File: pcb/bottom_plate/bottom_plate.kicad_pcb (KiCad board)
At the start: 2 copper layers, 285.8 x 126.1 mm, 44 parts

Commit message: Remove redundant ESD protection from bottom plate.
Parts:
- removed U_ESD_D1, U_ESD_D2, U_ESD_D3, U_ESD_D4, U_ESD_D5: CM1293A, Package_TO_SOT_SMD:SOT-23-6
- H1, H10, H11, H12, H2, H3, H4, H5, H6, H7, H8, H9: footprint MountingHole:MountingHole_2.2mm_M2 -> MountingHole:MountingHole_2.2mm_M2_Pad
- moved C1 4.36 mm to (239.4, 90.0)
- moved C2 4.36 mm to (241.9, 90.0)
- moved D_POW_1 4.36 mm to (242.9, 79.5)
- moved JP_CHG_1 4.36 mm to (241.9, 74.2)
- moved Q_POW_1 4.36 mm to (241.4, 84.5)
- moved R_CHG_1 4.36 mm to (238.3, 73.3)
- moved R_CHG_2 4.36 mm to (238.3, 68.3)
- moved R_POW_1 4.36 mm to (244.4, 90.0)
- moved U_CHG_1 4.36 mm to (238.4, 79.5)
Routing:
- net /Left/VCC: track 213.2 -> 171.5 mm, vias 6 -> 5
- net /Left/SCLK: track 181.1 -> 141.4 mm, vias 4 -> 5
- net /Right/CS_DIS2: track 60.9 -> 29.0 mm
- net /Left/MISO: track 175.8 -> 145.1 mm, vias 4 -> 5
- net /Left/VDD: track 189.8 -> 217.0 mm, vias 8 -> 5
- net /Left/CS_DIS2: track 120.2 -> 98.2 mm, vias 2 -> 0
- net /Left/GND: track 69.0 -> 48.4 mm, vias 22 -> 12
- net /Left/D-: track 112.0 -> 98.4 mm
- net /Left/MOSI: track 161.2 -> 148.4 mm, vias 6 -> 5
- net /Right/MISO: track 70.4 -> 60.2 mm
- net /Left/RST: track 164.8 -> 155.3 mm
- net /Left/SDA: track 145.1 -> 154.5 mm, vias 6 -> 5
- net /Left/D+: track 107.5 -> 98.4 mm
- net /Right/VDD: track 47.8 -> 40.1 mm
- net /Left/CS_PMW2: track 124.1 -> 117.2 mm, vias 2 -> 0
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
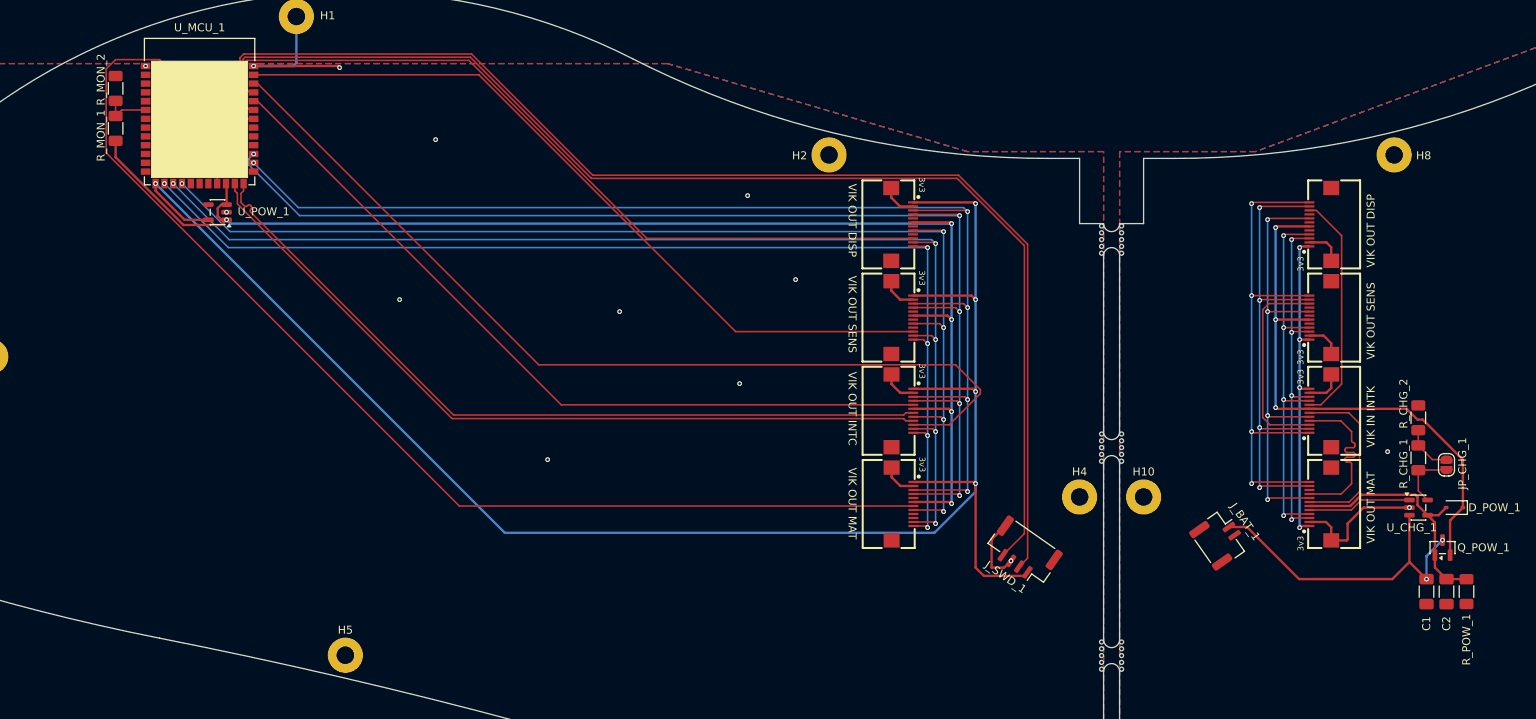
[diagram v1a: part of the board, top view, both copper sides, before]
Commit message: Standardize on 0805 footprint for passive components.
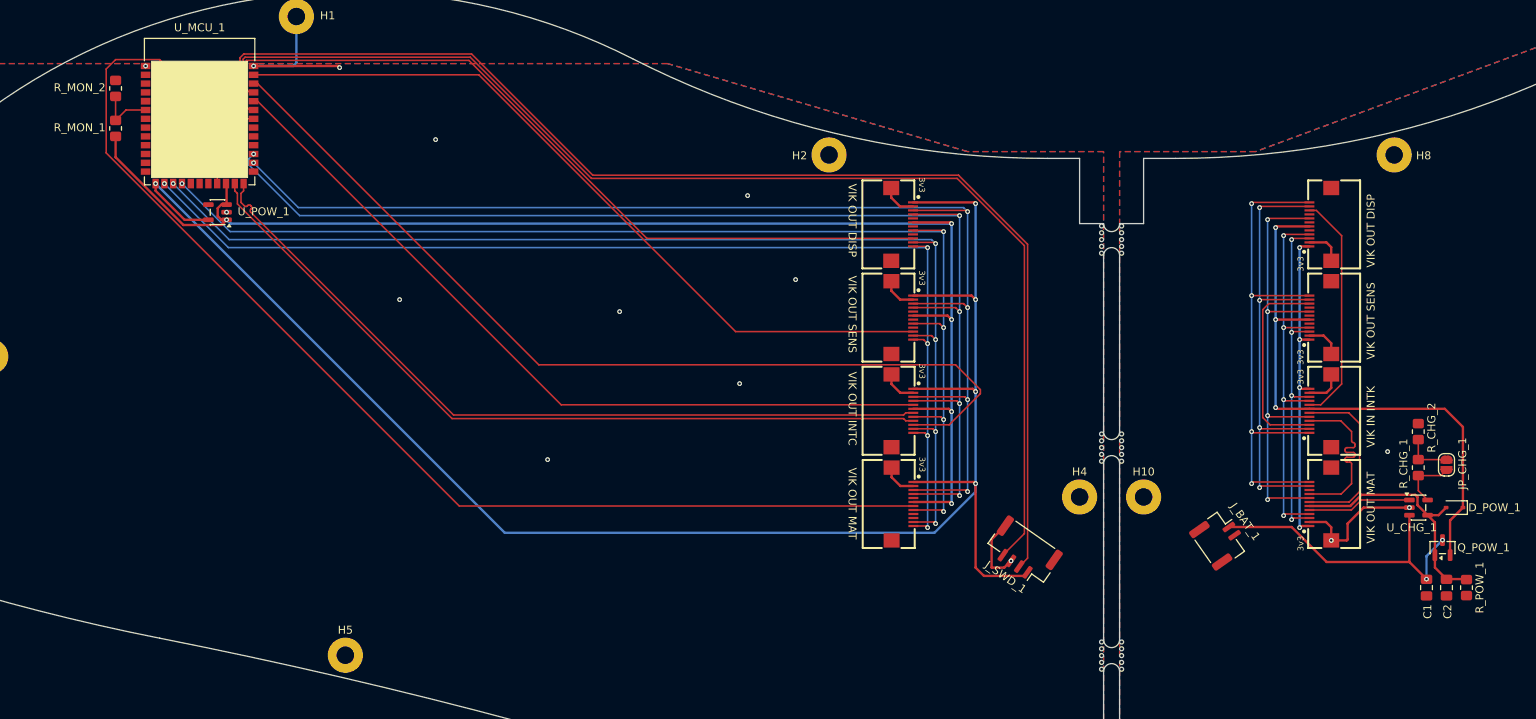
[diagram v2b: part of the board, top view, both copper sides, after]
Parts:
- C1, C2: footprint Capacitor_SMD:C_1206_3216Metric_Pad1.33x1.80mm_HandSolder -> Capacitor_SMD:C_0805_2012Metric_Pad1.18x1.45mm_HandSolder
- R_CHG_1, R_CHG_2, R_MON_1, R_MON_2, R_POW_1: footprint Resistor_SMD:R_1206_3216Metric_Pad1.30x1.75mm_HandSolder -> Resistor_SMD:R_0805_2012Metric_Pad1.20x1.40mm_HandSolder
- U_POW_1: value XC6220B331MR -> TLV75733PDYDR
- moved R_CHG_2 1.72 mm to (238.3, 70.0)
- moved R_CHG_1 1.22 mm to (238.3, 74.5)
- moved C1 0.50 mm to (239.4, 89.5)
- moved C2 0.50 mm to (241.9, 89.5)
- moved R_POW_1 0.50 mm to (244.4, 89.5)
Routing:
- net /Right/VCC: track 69.7 -> 72.1 mm
- net /Right/VBAT: track 40.7 -> 39.0 mm
- net /Left/BATT_MON: track 5.96 -> 7.29 mm
- net /Left/VCC: track 171.5 -> 172.0 mm
- net /Right/GND: vias 2 -> 3

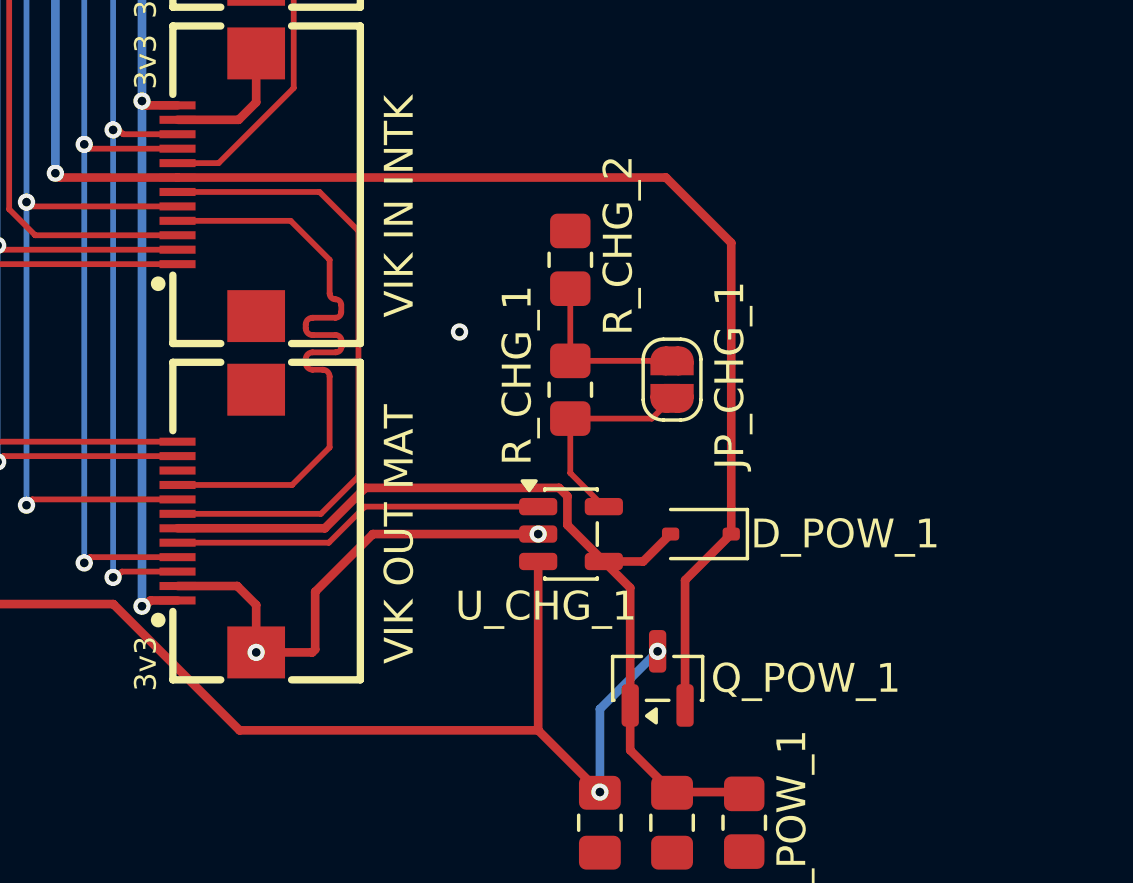
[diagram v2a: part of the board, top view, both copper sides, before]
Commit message: Correct Schottky diode footprint from SOD-323 to SOD-123.
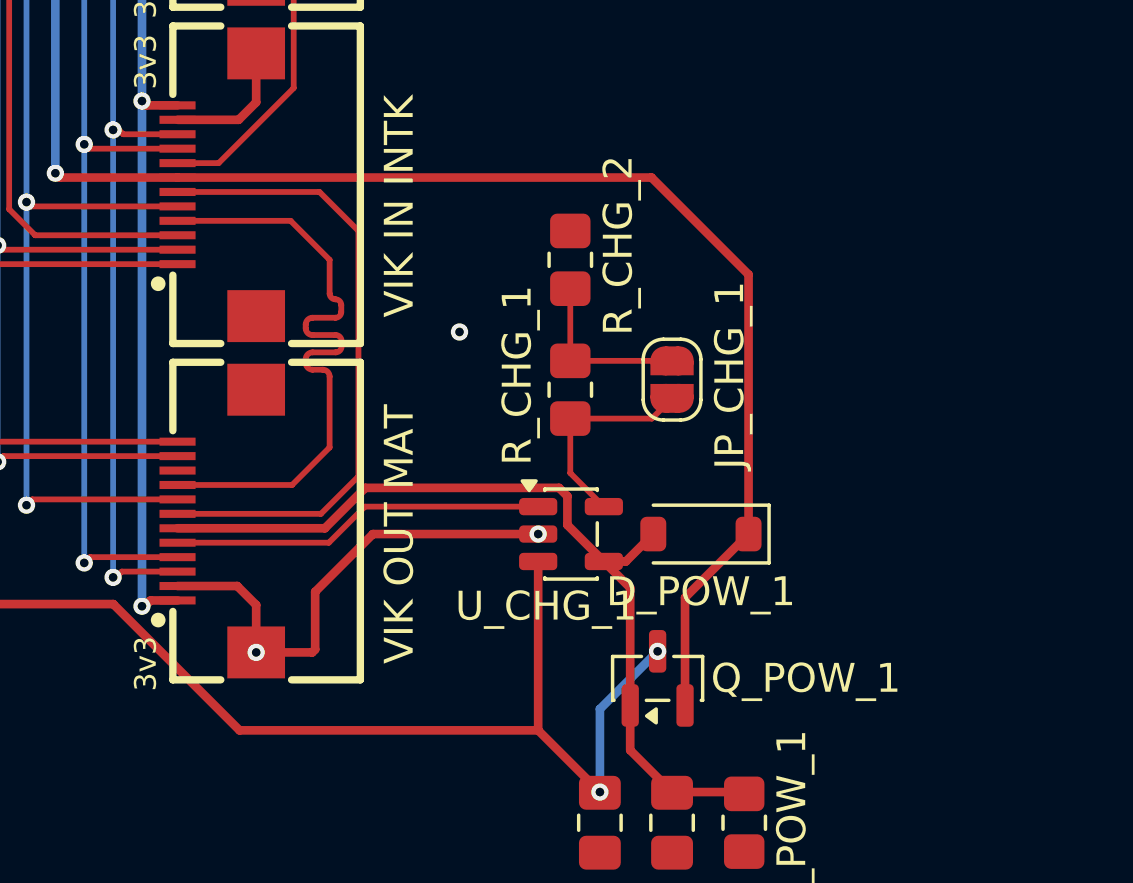
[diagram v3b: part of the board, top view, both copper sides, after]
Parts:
- D_POW_1: footprint Diode_SMD:D_SOD-323 -> Diode_SMD:D_SOD-123
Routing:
- net /Right/VUSB: track 31.2 -> 30.6 mm
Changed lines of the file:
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@@
 		(embedded_fonts no)
 	)
-	(footprint "Diode_SMD:D_SOD-323"
+	(footprint "Diode_SMD:D_SOD-123"
 		(layer "F.Cu")
 		(at 242.8625 79.5 180)
-		(descr "SOD-323")
-		(tags "SOD-323")
+		(descr "SOD-123")
+		(tags "SOD-123")
 		(property "Reference" "D_POW_1"
-			(at -5 0 0)
+			(at 0 -2 180)
 			(layer "F.SilkS")
 			(effects
@@
 		)
 		(property "Value" "1N5819WS"
-			(at -1.1375 1.9 0)
+			(at 0 2.1 180)
 			(layer "F.Fab")
 			(effects
@@
 		(duplicate_pad_numbers_are_jumpers no)
 		(fp_line
-			(start -1.61 0.85)
-			(end 1.05 0.85)
+			(start -2.36 1)
+			(end 1.65 1)
 			(stroke
 				(width 0.12)
@@
 		)
 		(fp_line
-			(start -1.61 -0.85)
-			(end 1.05 -0.85)
+			(start -2.36 -1)
+			(end 1.65 -1)
 			(stroke
 				(width 0.12)
@@
 		)
 		(fp_line
-			(start -1.61 -0.85)
-			(end -1.61 0.85)
+			(start -2.36 -1)
+			(end -2.36 1)
 			(stroke
 				(width 0.12)
@@
 		)
 		(fp_line
-			(start 1.6 -0.95)
-			(end 1.6 0.95)
+			(start 2.35 1.15)
+			(end -2.35 1.15)
 			(stroke
 				(width 0.05)
@@
 		)
 		(fp_line
-			(start -1.6 0.95)
-			(end 1.6 0.95)
+			(start 2.35 -1.15)
+			(end 2.35 1.15)
 			(stroke
 				(width 0.05)
@@
 		)
 		(fp_line
-			(start -1.6 -0.95)
-			(end 1.6 -0.95)
+			(start -2.35 -1.15)
+			(end 2.35 -1.15)
 			(stroke
 				(width 0.05)
@@
 		)
 		(fp_line
-			(start -1.6 -0.95)
-			(end -1.6 0.95)
+			(start -2.35 -1.15)
+			(end -2.35 1.15)
 			(stroke
 				(width 0.05)
@@
 		)
 		(fp_line
-			(start 0.9 0.7)
-			(end -0.9 0.7)
+			(start 1.4 0.9)
+			(end -1.4 0.9)
 			(stroke
 				(width 0.1)
@@
 		)
 		(fp_line
-			(start 0.9 -0.7)
-			(end 0.9 0.7)
+			(start 1.4 -0.9)
+			(end 1.4 0.9)
 			(stroke
 				(width 0.1)
@@
 		)
 		(fp_line
-			(start 0.2 0.35)
-			(end -0.3 0)
+			(start 0.25 0.4)
+			(end -0.35 0)
 			(stroke
 				(width 0.1)
@@
 		)
 		(fp_line
-			(start 0.2 0)
-			(end 0.45 0)
+			(start 0.25 0)
+			(end 0.75 0)
 			(stroke
 				(width 0.1)
@@
 		)
 		(fp_line
-			(start 0.2 -0.35)
-			(end 0.2 0.35)
+			(start 0.25 -0.4)
+			(end 0.25 0.4)
 			(stroke
 				(width 0.1)
@@
 		)
 		(fp_line
-			(start -0.3 0)
-			(end 0.2 -0.35)
+			(start -0.35 0)
+			(end 0.25 -0.4)
 			(stroke
 				(width 0.1)
@@
 		)
 		(fp_line
-			(start -0.3 0)
-			(end -0.5 0)
+			(start -0.35 0)
+			(end -0.35 0.55)
 			(stroke
 				(width 0.1)
@@
 		)
 		(fp_line
-			(start -0.3 -0.35)
-			(end -0.3 0.35)
+			(start -0.35 0)
+			(end -0.35 -0.55)
 			(stroke
 				(width 0.1)
@@
 		)
 		(fp_line
-			(start -0.9 0.7)
-			(end -0.9 -0.7)
+			(start -0.75 0)
+			(end -0.35 0)
 			(stroke
 				(width 0.1)
@@
 		)
 		(fp_line
-			(start -0.9 -0.7)
-			(end 0.9 -0.7)
+			(start -1.4 0.9)
+			(end -1.4 -0.9)
+			(stroke
+				(width 0.1)
+				(type solid)
+			)
+			(layer "F.Fab")
+		)
+		(fp_line
+			(start -1.4 -0.9)
+			(end 1.4 -0.9)
 			(stroke
 				(width 0.1)
@@
 		)
 		(fp_text user "${REFERENCE}"
-			(at -5 0 0)
+			(at 0 -2 180)
 			(layer "F.Fab")
 			(effects
@@
 		)
 		(pad "1" smd roundrect
-			(at -1.05 0 180)
-			(size 0.6 0.45)
+			(at -1.65 0 180)
+			(size 0.9 1.2)
 			(layers "F.Cu" "F.Mask" "F.Paste")
 			(roundrect_rratio 0.25)
@@
 		)
 		(pad "2" smd roundrect
-			(at 1.05 0 180)
-			(size 0.6 0.45)
+			(at 1.65 0 180)
+			(size 0.9 1.2)
 			(layers "F.Cu" "F.Mask" "F.Paste")
 			(roundrect_rratio 0.25)
@@
 		)
 		(embedded_fonts no)
-		(model "${KICAD10_3DMODEL_DIR}/Diode_SMD.3dshapes/D_SOD-323.step"
+		(model "${KICAD10_3DMODEL_DIR}/Diode_SMD.3dshapes/D_SOD-123.step"
 			(offset
 				(xyz 0 0 0)
@@
 	)
 	(segment
-		(start 229.836396 79.3)
-		(end 231.236396 77.9)
+		(start 239.5 80.45)
+		(end 240.2625 80.45)
 		(width 0.3)
 		(layer "F.Cu")
@@
 	)
 	(segment
-		(start 239.5 80.45)
-		(end 240.8625 80.45)
+		(start 229.836396 79.3)
+		(end 231.236396 77.9)
 		(width 0.3)
 		(layer "F.Cu")
@@
 	)
 	(segment
-		(start 240.8625 80.45)
-		(end 241.8125 79.5)
+		(start 240.2625 80.45)
+		(end 241.2125 79.5)
 		(width 0.3)
 		(layer "F.Cu")
@@
 	)
 	(segment
-		(start 242.3125 85.4375)
-		(end 242.3125 81.1)
+		(start 224.732 56.00016)
+		(end 220.50016 56.00016)
 		(width 0.3)
 		(layer "F.Cu")
@@
 	)
 	(segment
-		(start 224.732 56.00016)
-		(end 220.50016 56.00016)
+		(start 224.732 44.350238)
+		(end 220.649762 44.350238)
 		(width 0.3)
 		(layer "F.Cu")
@@
 	)
 	(segment
-		(start 224.732 44.350238)
-		(end 220.649762 44.350238)
+		(start 241.15008 67.15008)
+		(end 224.732 67.15008)
 		(width 0.3)
 		(layer "F.Cu")
@@
 	)
 	(segment
-		(start 242.3125 81.1)
-		(end 243.9125 79.5)
+		(start 244.5125 70.5125)
+		(end 241.15008 67.15008)
 		(width 0.3)
 		(layer "F.Cu")
@@
 	)
 	(segment
-		(start 224.732 67.15008)
-		(end 241.65008 67.15008)
+		(start 242.3125 85.4375)
+		(end 242.3125 81.7)
 		(width 0.3)
 		(layer "F.Cu")
@@
 	)
 	(segment
-		(start 243.9125 69.4125)
-		(end 243.9125 79.5)
+		(start 242.3125 81.7)
+		(end 244.5125 79.5)
 		(width 0.3)
 		(layer "F.Cu")
@@
 	)
 	(segment
-		(start 224.732 67.15008)
-		(end 220.65008 67.15008)
+		(start 244.5125 79.5)
+		(end 244.5125 70.5125)
 		(width 0.3)
 		(layer "F.Cu")
@@
 	)
 	(segment
-		(start 241.65008 67.15008)
-		(end 243.9125 69.4125)
+		(start 224.732 67.15008)
+		(end 220.65008 67.15008)
 		(width 0.3)
 		(layer "F.Cu")

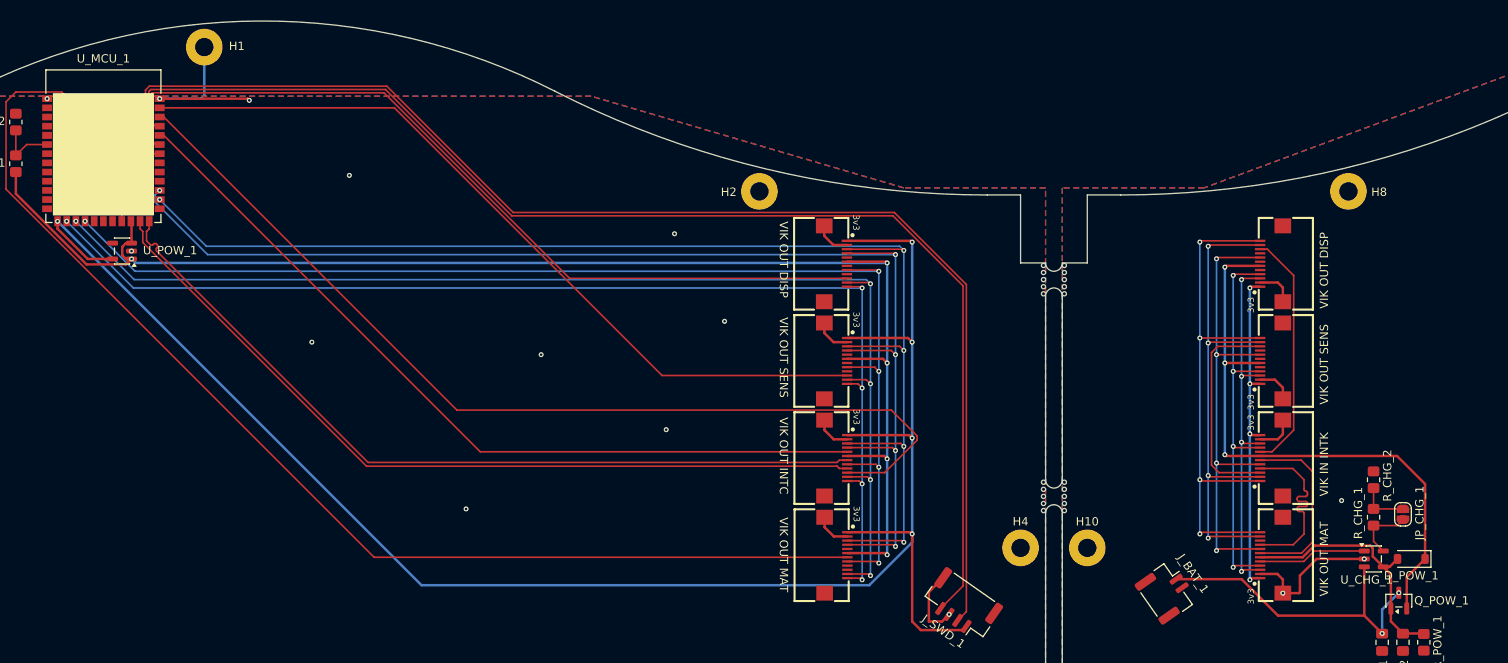
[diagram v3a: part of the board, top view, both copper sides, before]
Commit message: Update KiCAD projects to use new library locations.
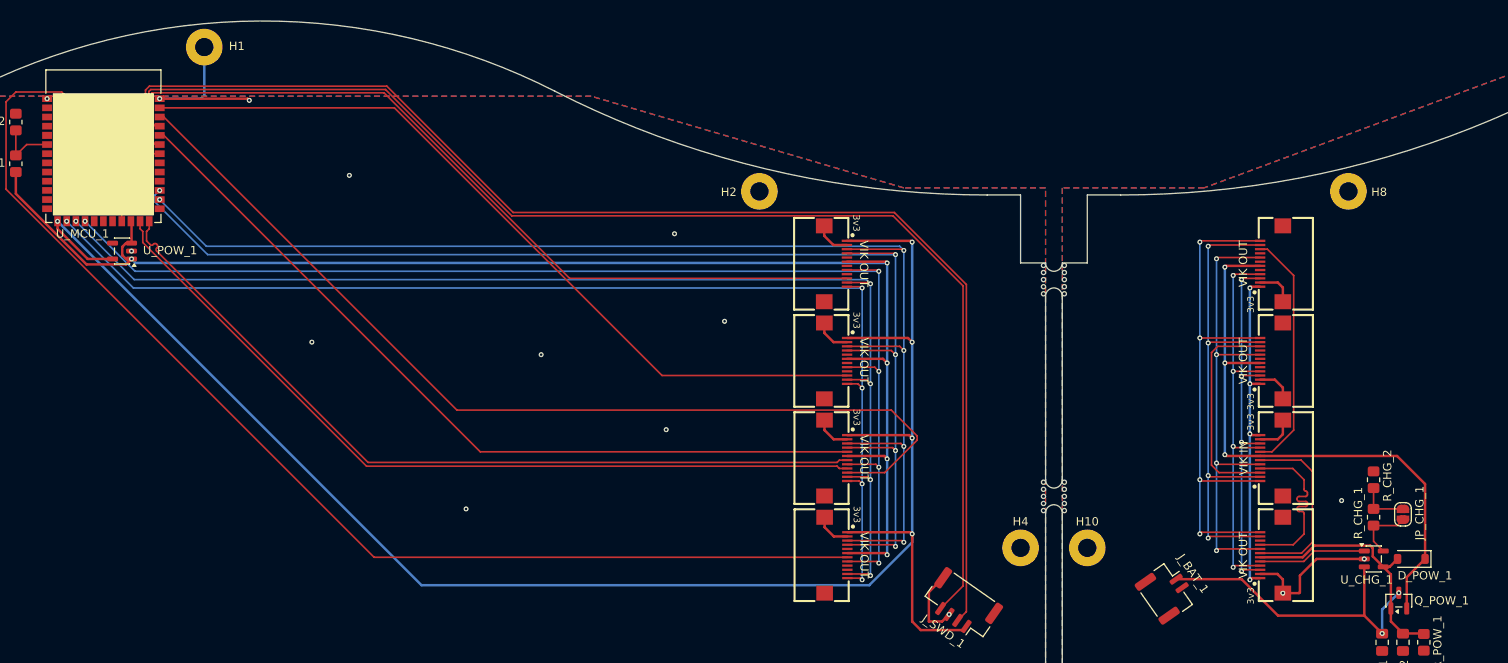
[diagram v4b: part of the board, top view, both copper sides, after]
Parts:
- J_VIK_IN_INTC_1: footprint vik:vik-module-connector-horizontal -> footprints:vik-module-connector-horizontal
- J_VIK_OUT_DISP_1, J_VIK_OUT_DISP_2, J_VIK_OUT_INTC_1, J_VIK_OUT_SENS_1, J_VIK_OUT_SENS_2, J_VIK_OUT_SW_1, J_VIK_OUT_SW_2: footprint vik:vik-keyboard-connector-horizontal -> footprints:vik-keyboard-connector-horizontal
- U_MCU_1: footprint mcu:holyiot-18010-no-underside -> footprints:holyiot-18010-no-underside
